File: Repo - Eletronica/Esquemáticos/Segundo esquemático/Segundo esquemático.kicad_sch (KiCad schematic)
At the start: 31 parts, among them M1 Motor Esquerdo, M2 Motor Direito, Q1 BC547, Q2 BC547, SW1 Chave/Interruptor, SW2 Chave/Interruptor, U2 Medidor de Corrente ACS712, U3 Sensor 1 TCRT500, U4 Sensor 2 TCRT500, U5 Sensor 3 TCRT500, U6 Sensor 4 TCRT500

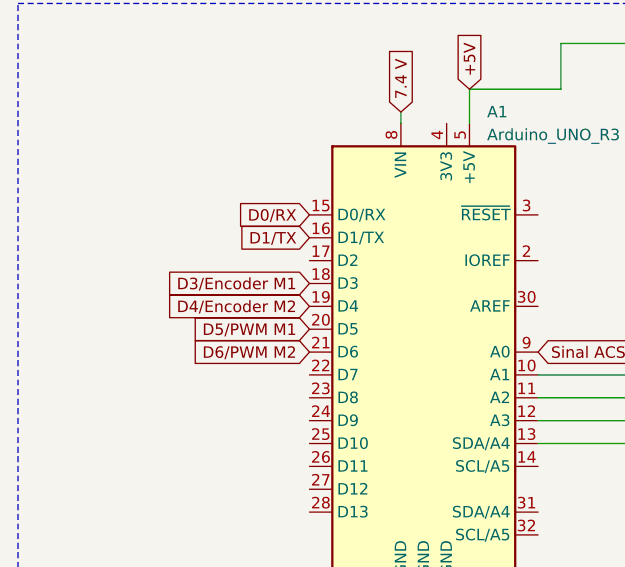
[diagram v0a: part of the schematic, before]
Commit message: Atualização
Alterei os valores de resistores de 3k para 3k3. Comecei a construção do firmware do projeto
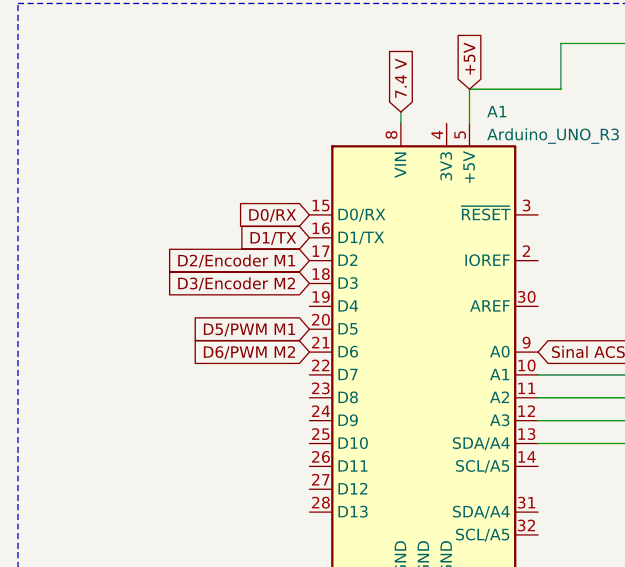
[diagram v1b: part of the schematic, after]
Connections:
- net D3/Encoder M1: no longer A1.18 (D3)
- net D4/Encoder M2: no longer A1.19 (D4)
- net D2/Encoder M1: now reaches A1.17 (D2)
- new net: U2.8 (VCC), U8. (Vcc), U9. (Vcc)
- new net D3/Encoder M2: A1.18 (D3)
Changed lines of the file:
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@@
     )
   )
-  (global_label "D3{slash}Encoder M1" (shape input) (at 49.53 49.53 180) (fields_autoplaced)
+  (global_label "D2{slash}Encoder M1" (shape input) (at 49.53 46.99 180) (fields_autoplaced)
     (effects (font (size 1.27 1.27)) (justify right))
-    (property "Intersheetrefs" "${INTERSHEET_REFS}" (at 31.6263 49.53 0)
+    (property "Intersheetrefs" "${INTERSHEET_REFS}" (at 31.6263 46.99 0)
       (effects (font (size 1.27 1.27)) (justify right) hide)
     )
@@
     )
   )
-  (global_label "D4{slash}Encoder M2" (shape input) (at 49.53 52.07 180) (fields_autoplaced)
+  (global_label "D3{slash}Encoder M2" (shape input) (at 49.53 49.53 180) (fields_autoplaced)
     (effects (font (size 1.27 1.27)) (justify right))
-    (property "Intersheetrefs" "${INTERSHEET_REFS}" (at 31.6263 52.07 0)
+    (property "Intersheetrefs" "${INTERSHEET_REFS}" (at 31.6263 49.53 0)
       (effects (font (size 1.27 1.27)) (justify right) hide)
     )

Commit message: att
att dos esquemáticos
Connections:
- new net: U2.8 (VCC), U8. (Vcc), U9. (Vcc)
